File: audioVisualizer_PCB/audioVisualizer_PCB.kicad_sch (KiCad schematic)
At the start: 38 parts, among them J1 USB_C_16P, J2 SWD_DEBUG, J3 SPI_LED_MATRIX, U1 AMS1117-3.3, U7 STM32F401CCUx, Y1 ASE-25MHz

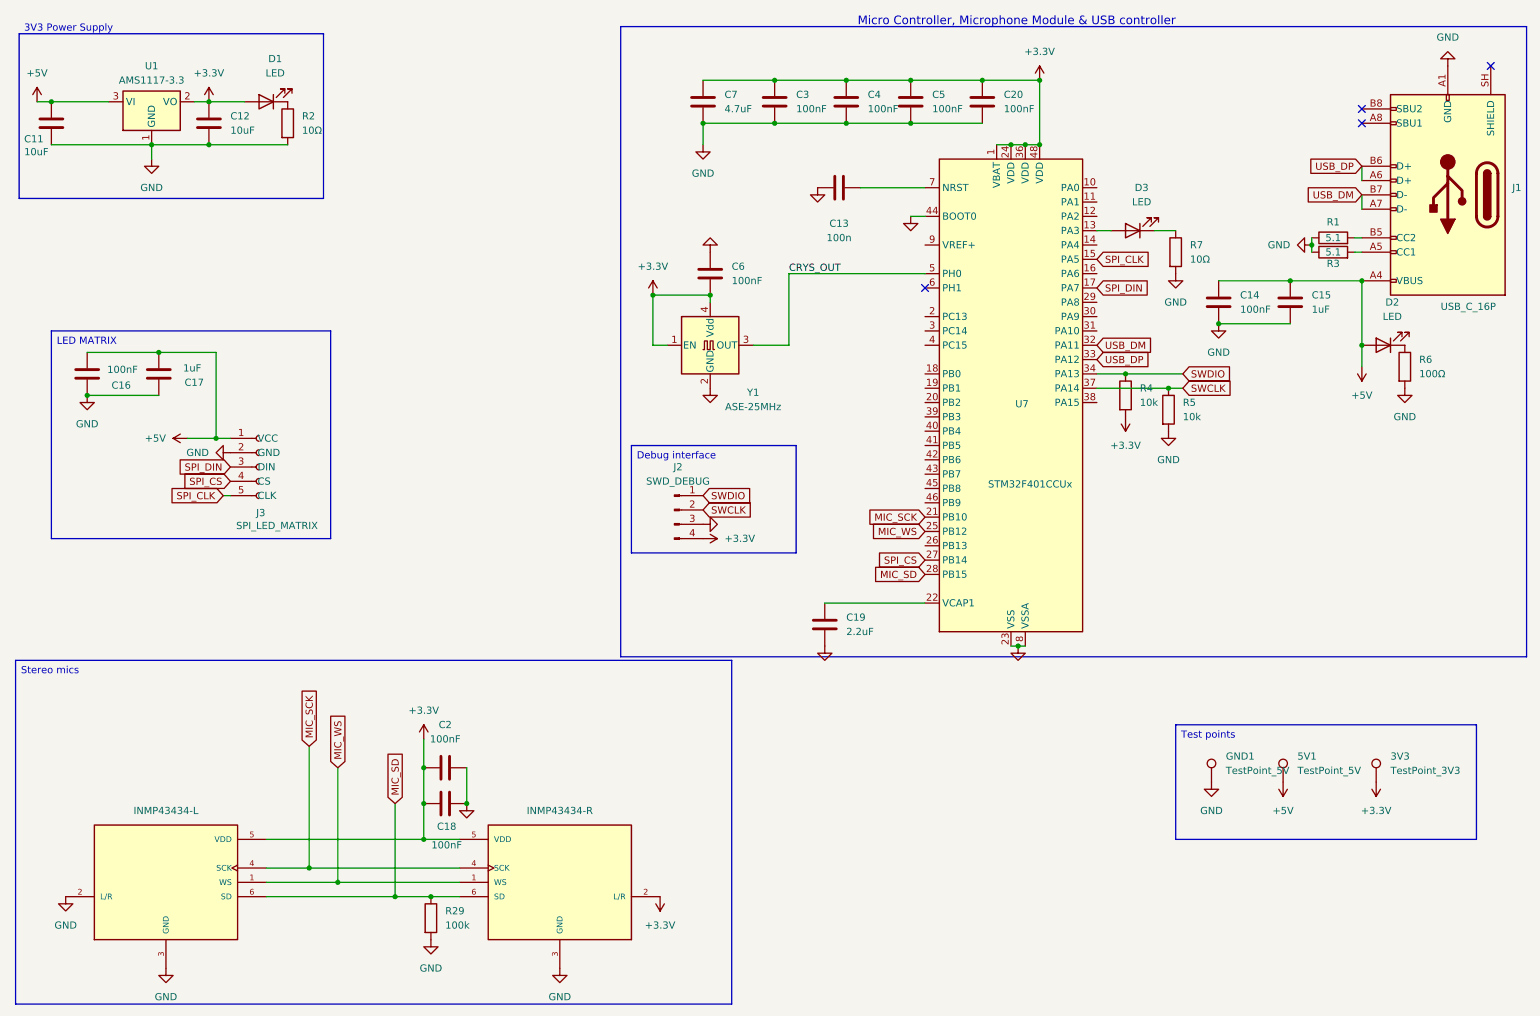
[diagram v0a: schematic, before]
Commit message: manually routed the tracks; switch LEFT/RIGHT mic
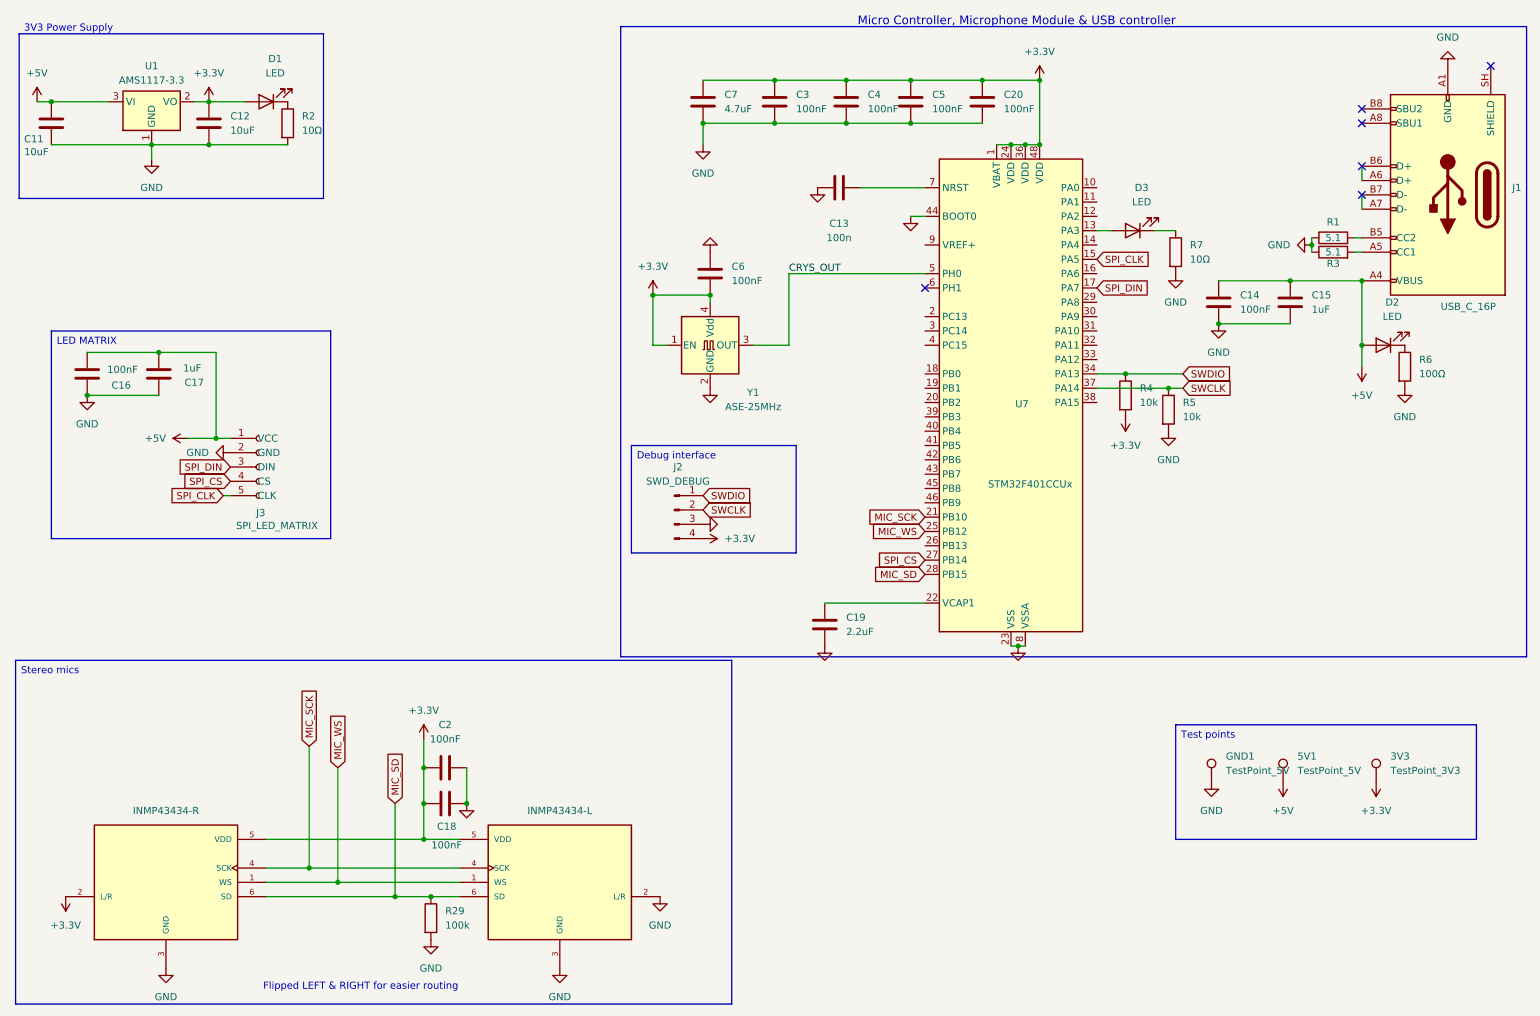
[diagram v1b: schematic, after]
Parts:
- MK-L1: value INMP43434-L -> INMP43434-R
- MK-R1: value INMP43434-R -> INMP43434-L
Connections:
- net +3.3V: now also MK-L1.2 (L/R); no longer MK-R1.2 (L/R)
- net GND: now also MK-R1.2 (L/R); no longer MK-L1.2 (L/R)
- net USB_DM: no longer names the net of J1.A7 (D-), J1.B7 (D-)
- net USB_DM: no longer U7.32 (PA11)
- net USB_DP: no longer names the net of J1.A6 (D+), J1.B6 (D+)
- net USB_DP: no longer U7.33 (PA12)
- no-connect marks 4 -> 6
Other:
- note added: "Flipped LEFT & RIGHT for easier routing"
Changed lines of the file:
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@@
 		)
 	)
+	(text "Flipped LEFT & RIGHT for easier routing"
+		(exclude_from_sim no)
+		(at 76.454 184.912 0)
+		(effects
+			(font
+				(size 1.27 1.27)
+			)
+		)
+	)
 	(text_box "Test points\n"
 		(exclude_from_sim no)
@@
 		(at 254 29.21)
 	)
+	(no_connect
+		(at 254 44.45)
+	)
+	(no_connect
+		(at 254 39.37)
+	)
 	(wire
 		(pts
@@
 		)
 	)
-	(global_label "USB_DP"
-		(shape input)
-		(at 254 39.37 180)
-		(fields_autoplaced yes)
-		(effects
-			(font
-				(size 1.27 1.27)
-			)
-			(justify right)
-		)
-		(property "Intersheetrefs" "${INTERSHEET_REFS}"
-			(at 243.6972 39.37 0)
-			(hide yes)
-			(show_name no)
-			(do_not_autoplace no)
-			(effects
-				(font
-					(size 1.27 1.27)
-				)
-				(justify right)
-			)
-		)
-	)
 	(global_label "SPI_CS"
 		(shape input)
@@
 		)
 	)
-	(global_label "USB_DM"
-		(shape input)
-		(at 254 44.45 180)
-		(fields_autoplaced yes)
-		(effects
-			(font
-				(size 1.27 1.27)
-			)
-			(justify right)
-		)
-		(property "Intersheetrefs" "${INTERSHEET_REFS}"
-			(at 243.5158 44.45 0)
-			(hide yes)
-			(show_name no)
-			(do_not_autoplace no)
-			(effects
-				(font
-					(size 1.27 1.27)
-				)
-				(justify right)
-			)
-		)
-	)
 	(global_label "SWDIO"
 		(shape input)
@@
 		)
 	)
-	(global_label "USB_DM"
-		(shape input)
-		(at 207.01 71.12 0)
-		(fields_autoplaced yes)
-		(effects
-			(font
-				(size 1.27 1.27)
-			)
-			(justify left)
-		)
-		(property "Intersheetrefs" "${INTERSHEET_REFS}"
-			(at 217.4942 71.12 0)
-			(hide yes)
-			(show_name no)
-			(do_not_autoplace no)
-			(effects
-				(font
-					(size 1.27 1.27)
-				)
-				(justify left)
-			)
-		)
-	)
 	(global_label "SPI_DIN"
 		(shape input)
@@
 		)
 	)
-	(global_label "USB_DP"
-		(shape input)
-		(at 207.01 73.66 0)
-		(fields_autoplaced yes)
-		(effects
-			(font
-				(size 1.27 1.27)
-			)
-			(justify left)
-		)
-		(property "Intersheetrefs" "${INTERSHEET_REFS}"
-			(at 217.3128 73.66 0)
-			(hide yes)
-			(show_name no)
-			(do_not_autoplace no)
-			(effects
-				(font
-					(size 1.27 1.27)
-				)
-				(justify left)
-			)
-		)
-	)
 	(global_label "MIC_SCK"
 		(shape input)
@@
 	(symbol
 		(lib_id "power:+3.3V")
+		(at 24.13 168.91 180)
+		(unit 1)
+		(body_style 1)
+		(exclude_from_sim no)
+		(in_bom yes)
+		(on_board yes)
+		(in_pos_files yes)
+		(dnp no)
+		(fields_autoplaced yes)
+		(property "Reference" "#PWR037"
+			(at 24.13 165.1 0)
+			(hide yes)
+			(show_name no)
+			(do_not_autoplace no)
+			(effects
+				(font
+					(size 1.27 1.27)
+				)
+			)
+		)
+		(property "Value" "+3.3V"
+			(at 24.13 173.99 0)
+			(show_name no)
+			(do_not_autoplace no)
+			(effects
+				(font
+					(size 1.27 1.27)
+				)
+			)
+		)
+		(property "Footprint" ""
+			(at 24.13 168.91 0)
+			(hide yes)
+			(show_name no)
+			(do_not_autoplace no)
+			(effects
+				(font
+					(size 1.27 1.27)
+				)
+			)
+		)
+		(property "Datasheet" ""
+			(at 24.13 168.91 0)
+			(hide yes)
+			(show_name no)
+			(do_not_autoplace no)
+			(effects
+				(font
+					(size 1.27 1.27)
+				)
+			)
+		)
+		(property "Description" "Power symbol creates a global label with name \"+3.3V\""
+			(at 24.13 168.91 0)
+			(hide yes)
+			(show_name no)
+			(do_not_autoplace no)
+			(effects
+				(font
+					(size 1.27 1.27)
+				)
+			)
+		)
+		(pin "1"
+		)
+		(instances
+			(project "audioVisualizer_PCB"
+				(path "/8779f4c0-fa76-4e9c-9285-12099bba0fb4"
+					(reference "#PWR037")
+					(unit 1)
+				)
+			)
+		)
+	)
+	(symbol
+		(lib_id "power:+3.3V")
 		(at 137.16 105.41 270)
 		(unit 1)
@@
 			)
 		)
-		(property "Value" "INMP43434-L"
+		(property "Value" "INMP43434-R"
 			(at 41.91 153.67 0)
 			(show_name no)
@@
 			)
 		)
-		(property "Value" "INMP43434-R"
+		(property "Value" "INMP43434-L"
 			(at 111.76 153.67 0)
 			(show_name no)
@@
 	)
 	(symbol
-		(lib_id "power:+3.3V")
-		(at 129.54 168.91 180)
-		(unit 1)
-		(body_style 1)
-		(exclude_from_sim no)
-		(in_bom yes)
-		(on_board yes)
-		(in_pos_files yes)
-		(dnp no)
-		(fields_autoplaced yes)
-		(property "Reference" "#PWR037"
-			(at 129.54 165.1 0)
-			(hide yes)
-			(show_name no)
-			(do_not_autoplace no)
-			(effects
-				(font
-					(size 1.27 1.27)
-				)
-			)
-		)
-		(property "Value" "+3.3V"
-			(at 129.54 173.99 0)
-			(show_name no)
-			(do_not_autoplace no)
-			(effects
-				(font
-					(size 1.27 1.27)
-				)
-			)
-		)
-		(property "Footprint" ""
-			(at 129.54 168.91 0)
-			(hide yes)
-			(show_name no)
-			(do_not_autoplace no)
-			(effects
-				(font
-					(size 1.27 1.27)
-				)
-			)
-		)
-		(property "Datasheet" ""
-			(at 129.54 168.91 0)
-			(hide yes)
-			(show_name no)
-			(do_not_autoplace no)
-			(effects
-				(font
-					(size 1.27 1.27)
-				)
-			)
-		)
-		(property "Description" "Power symbol creates a global label with name \"+3.3V\""
-			(at 129.54 168.91 0)
-			(hide yes)
-			(show_name no)
-			(do_not_autoplace no)
-			(effects
-				(font
-					(size 1.27 1.27)
-				)
-			)
-		)
-		(pin "1"
-		)
-		(instances
-			(project "audioVisualizer_PCB"
-				(path "/8779f4c0-fa76-4e9c-9285-12099bba0fb4"
-					(reference "#PWR037")
-					(unit 1)
-				)
-			)
-		)
-	)
-	(symbol
 		(lib_id "Device:C")
 		(at 158.75 120.65 0)
@@
 	(symbol
 		(lib_id "power:GND")
-		(at 39.37 38.1 0)
+		(at 129.54 168.91 0)
 		(unit 1)
 		(body_style 1)
@@
 		(dnp no)
 		(fields_autoplaced yes)
-		(property "Reference" "#PWR019"
-			(at 39.37 44.45 0)
+		(property "Reference" "#PWR031"
+			(at 129.54 175.26 0)
 			(hide yes)
 			(show_name no)
@@
 		)
 		(property "Value" "GND"
-			(at 39.37 43.18 0)
+			(at 129.54 173.99 0)
 			(show_name no)
 			(do_not_autoplace no)
@@
 		)
 		(property "Footprint" ""
-			(at 39.37 38.1 0)
+			(at 129.54 168.91 0)
 			(hide yes)
 			(show_name no)
@@
 		)
 		(property "Datasheet" ""
-			(at 39.37 38.1 0)
+			(at 129.54 168.91 0)
 			(hide yes)
 			(show_name no)
@@
 		)
 		(property "Description" "Power symbol creates a global label with name \"GND\" , ground"
-			(at 39.37 38.1 0)
+			(at 129.54 168.91 0)
 			(hide yes)
 			(show_name no)
@@
 			(project "audioVisualizer_PCB"
 				(path "/8779f4c0-fa76-4e9c-9285-12099bba0fb4"
-					(reference "#PWR019")
+					(reference "#PWR031")
 					(unit 1)
 				)
@@
 	(symbol
 		(lib_id "power:GND")
-		(at 24.13 168.91 0)
+		(at 39.37 38.1 0)
 		(unit 1)
 		(body_style 1)
@@
 		(dnp no)
 		(fields_autoplaced yes)
-		(property "Reference" "#PWR035"
-			(at 24.13 175.26 0)
+		(property "Reference" "#PWR019"
+			(at 39.37 44.45 0)
 			(hide yes)
 			(show_name no)
@@
 		)
 		(property "Value" "GND"
-			(at 24.13 173.99 0)
+			(at 39.37 43.18 0)
 			(show_name no)
 			(do_not_autoplace no)
@@
 		)
 		(property "Footprint" ""
-			(at 24.13 168.91 0)
+			(at 39.37 38.1 0)
 			(hide yes)
 			(show_name no)
@@
 		)
 		(property "Datasheet" ""
-			(at 24.13 168.91 0)
+			(at 39.37 38.1 0)
 			(hide yes)
 			(show_name no)
@@
 		)
 		(property "Description" "Power symbol creates a global label with name \"GND\" , ground"
-			(at 24.13 168.91 0)
+			(at 39.37 38.1 0)
 			(hide yes)
 			(show_name no)
@@
 			(project "audioVisualizer_PCB"
 				(path "/8779f4c0-fa76-4e9c-9285-12099bba0fb4"
-					(reference "#PWR035")
+					(reference "#PWR019")
 					(unit 1)
 				)
